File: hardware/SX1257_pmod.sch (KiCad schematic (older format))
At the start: 47 parts, among them J1 Conn_02x06_Odd_Even, J2 SMA_F_RX, J3 SMA_F_TX, U1 SX1257, U2 SC18IS602B, Y1 36MHz 10ppm

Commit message: WIP
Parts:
- added U?: Si514, symbol Si514:Si514
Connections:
- net GND: now also U?.3 (GND)
- net XTB renamed OSC_CLK+
- net OSC_CLK+: now also U?.4 (CLK_+)
- new net +1V8: U?.6 (VDD)
- new net I2C_1V8_SCL: U?.2 (SCL)
- new net I2C_1V8_SDA: U?.1 (SDA)
- no-connect marks 1 -> 2
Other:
- note added: "TODO: 3V3 -> 1V8 LDO"
- note added: "TODO: Level shifting!\nhttps://www.nxp.com/docs/en/application-note/AN10441.pdf"
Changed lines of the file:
@@
 	10850 1000 10850 1100
 NoConn ~ 11550 1900
+$Comp
+L Si514:Si514 U?
+U 1 1 5C7B290D
+P 12400 3950
+F 0 "U?" H 12700 3450 50  0000 C CNN
+F 1 "Si514" H 12650 3550 50  0000 C CNN
+F 2 "" H 11950 4050 50  0001 C CNN
+F 3 "" H 11950 4050 50  0001 C CNN
+	1    12400 3950
+	1    0    0    -1
+$EndComp
+$Comp
+L power:GND #PWR?
+U 1 1 5C7B2B6A
+P 12400 4550
+F 0 "#PWR?" H 12400 4300 50  0001 C CNN
+F 1 "GND" H 12405 4377 50  0000 C CNN
+F 2 "" H 12400 4550 50  0001 C CNN
+F 3 "" H 12400 4550 50  0001 C CNN
+	1    12400 4550
+	1    0    0    -1
+$EndComp
+Wire Wire Line
+	12400 4550 12400 4350
+Wire Wire Line
+	12400 3250 12400 3450
+$Comp
+L power:+1V8 #PWR?
+U 1 1 5C7EB9B9
+P 12400 3250
+F 0 "#PWR?" H 12400 3100 50  0001 C CNN
+F 1 "+1V8" H 12415 3423 50  0000 C CNN
+F 2 "" H 12400 3250 50  0001 C CNN
+F 3 "" H 12400 3250 50  0001 C CNN
+	1    12400 3250
+	1    0    0    -1
+$EndComp
+Text Label 10850 3850 2    50   ~ 0
+I2C_SDA
+Text Label 10850 3950 2    50   ~ 0
+I2C_SCL
+Wire Wire Line
+	11750 3950 11950 3950
+Wire Wire Line
+	11950 3850 11750 3850
+Text Notes 9550 3650 0    50   ~ 0
+TODO: Level shifting!\nhttps://www.nxp.com/docs/en/application-note/AN10441.pdf
+NoConn ~ 12850 3850
+Text Label 13050 3950 0    50   ~ 0
+OSC_CLK+
+Text Label 13700 3950 0    50   ~ 0
+XTB
+Wire Wire Line
+	12850 3950 13700 3950
+Text Label 11750 3850 2    50   ~ 0
+I2C_1V8_SDA
+Text Label 11750 3950 2    50   ~ 0
+I2C_1V8_SCL
+Text Notes 12600 3200 0    50   ~ 0
+TODO: 3V3 -> 1V8 LDO
 $EndSCHEMATC

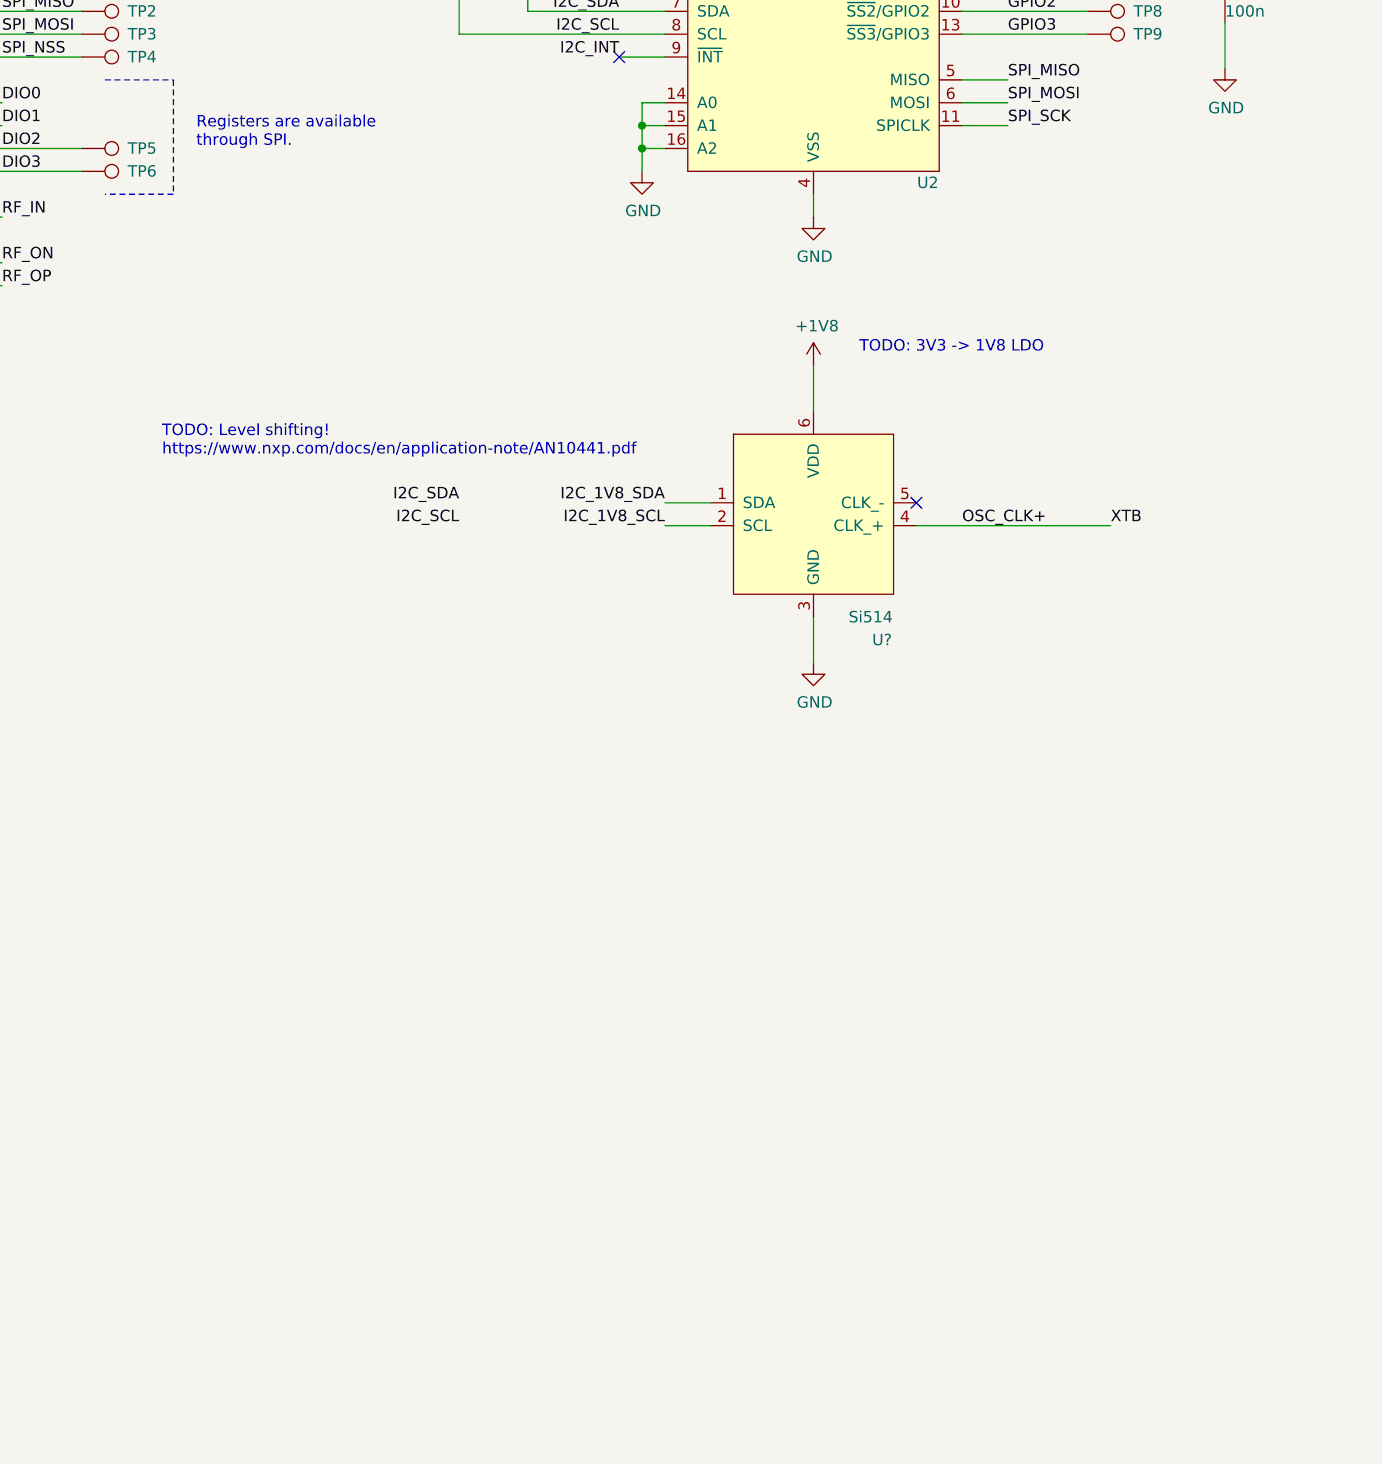
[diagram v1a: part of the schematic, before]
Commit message: Add I2C level shifter
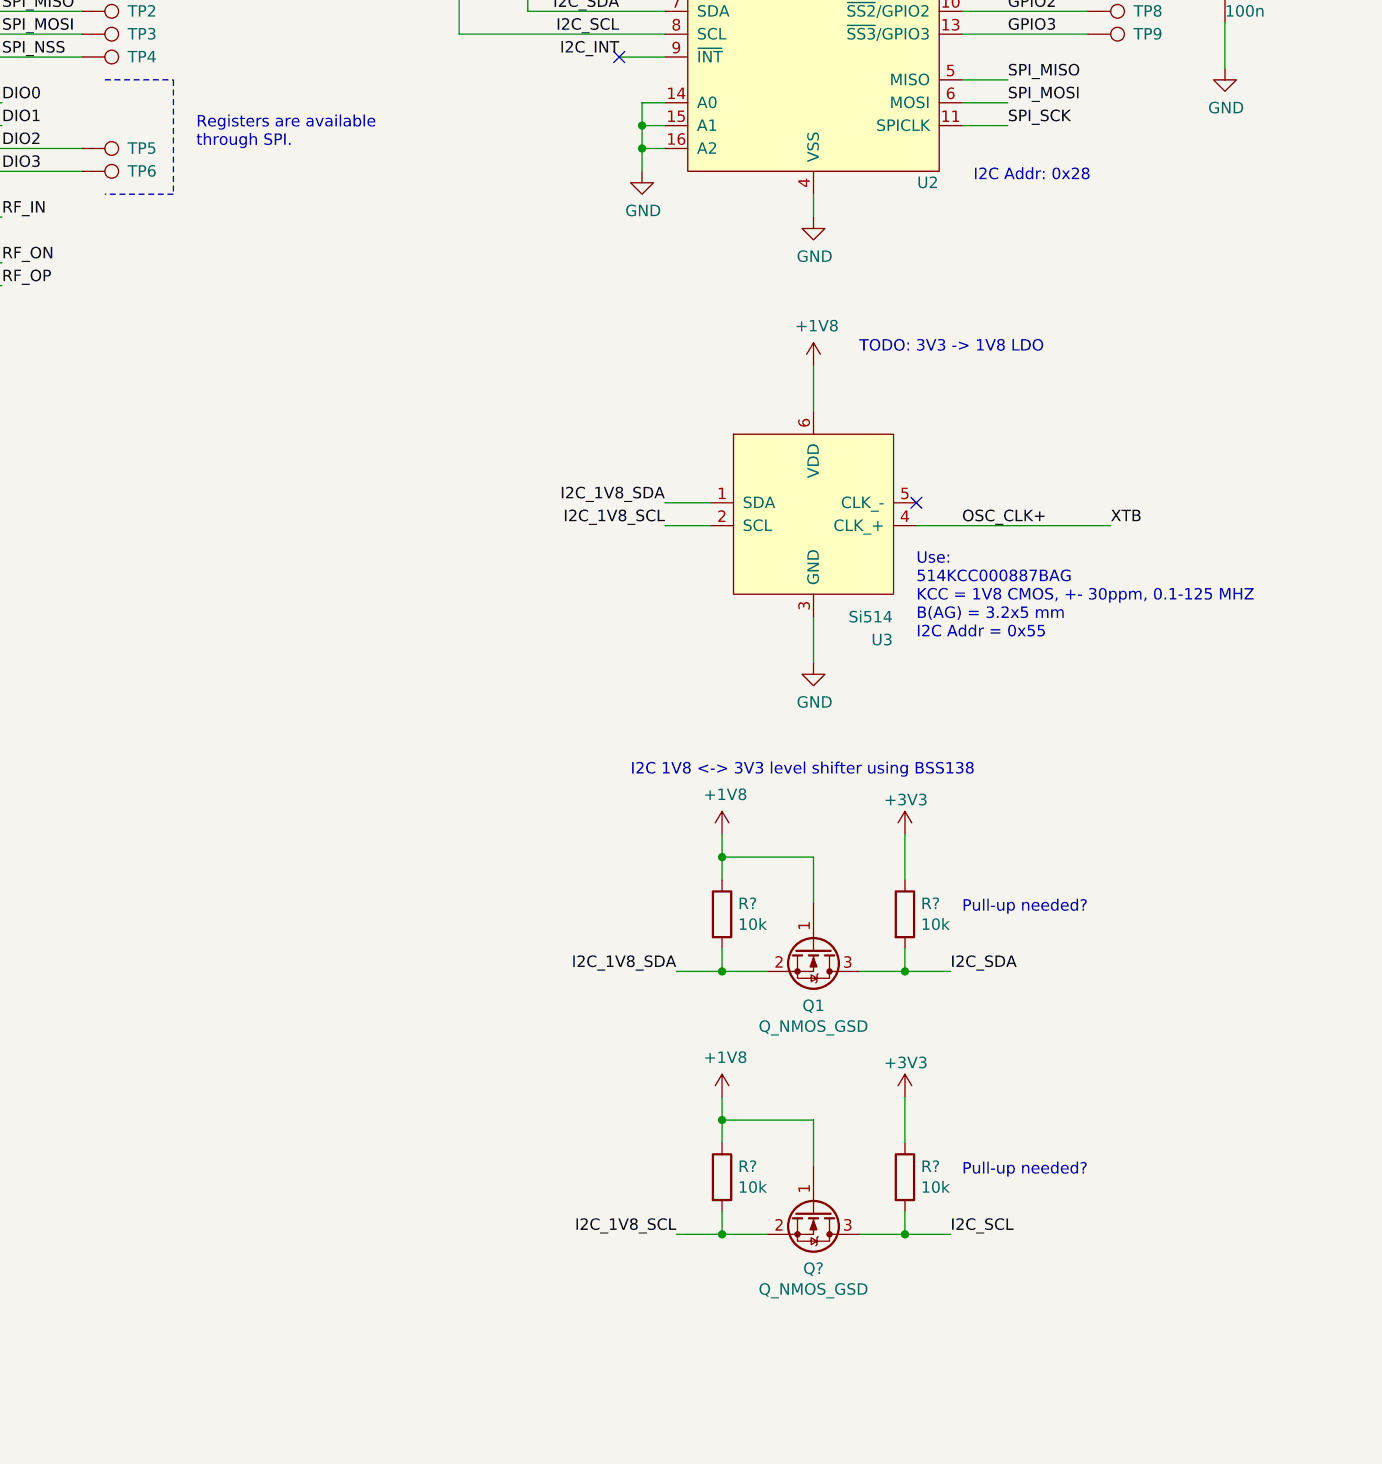
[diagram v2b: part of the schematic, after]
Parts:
- added Q1, Q?: Q_NMOS_GSD, Package_TO_SOT_SMD:SOT-23, symbol Device:Q_NMOS_GSD
- added R? (x4): 10k, Resistor_SMD:R_0603_1608Metric, symbol Device:R
- gave numbers to parts that had none: 1
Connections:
- net +1V8: now also Q1.1 (G), Q?.1 (G), R?.1, R?.1
- net +3V3: now also R?.1, R?.1
- net I2C_1V8_SCL: now also Q?.2 (S), R?.2
- net I2C_1V8_SDA: now also Q1.2 (S), R?.2
- net I2C_SCL: now also Q?.3 (D), R?.2
- net I2C_SDA: now also Q1.3 (D), R?.2
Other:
- note added: "I2C 1V8 <-> 3V3 level shifter using BSS138"
- note added: "I2C Addr: 0x28"
- note added: "Pull-up needed?"
- note added: "Use:\n514KCC000887BAG\nKCC = 1V8 CMOS, +- 30ppm, 0.1-125 MHZ\nB(AG) = 3.2x5 mm\nI2C Addr = 0x55"
- note removed: "TODO: Level shifting!\nhttps://www.nxp.com/docs/en/application-note/AN10441.pdf"
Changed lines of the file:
@@
 NoConn ~ 11550 1900
 $Comp
-L Si514:Si514 U?
+L Si514:Si514 U3
 U 1 1 5C7B290D
 P 12400 3950
-F 0 "U?" H 12700 3450 50  0000 C CNN
+F 0 "U3" H 12700 3450 50  0000 C CNN
 F 1 "Si514" H 12650 3550 50  0000 C CNN
 F 2 "" H 11950 4050 50  0001 C CNN
@@
 $EndComp
 $Comp
-L power:GND #PWR?
+L power:GND #PWR0103
 U 1 1 5C7B2B6A
 P 12400 4550
-F 0 "#PWR?" H 12400 4300 50  0001 C CNN
+F 0 "#PWR0103" H 12400 4300 50  0001 C CNN
 F 1 "GND" H 12405 4377 50  0000 C CNN
 F 2 "" H 12400 4550 50  0001 C CNN
@@
 	12400 3250 12400 3450
 $Comp
-L power:+1V8 #PWR?
+L power:+1V8 #PWR0104
 U 1 1 5C7EB9B9
 P 12400 3250
-F 0 "#PWR?" H 12400 3100 50  0001 C CNN
+F 0 "#PWR0104" H 12400 3100 50  0001 C CNN
 F 1 "+1V8" H 12415 3423 50  0000 C CNN
 F 2 "" H 12400 3250 50  0001 C CNN
@@
 	1    0    0    -1
 $EndComp
-Text Label 10850 3850 2    50   ~ 0
-I2C_SDA
-Text Label 10850 3950 2    50   ~ 0
+Text Label 13000 7050 0    50   ~ 0
 I2C_SCL
 Wire Wire Line
@@
 Wire Wire Line
 	11950 3850 11750 3850
-Text Notes 9550 3650 0    50   ~ 0
-TODO: Level shifting!\nhttps://www.nxp.com/docs/en/application-note/AN10441.pdf
 NoConn ~ 12850 3850
 Text Label 13050 3950 0    50   ~ 0
@@
 Text Notes 12600 3200 0    50   ~ 0
 TODO: 3V3 -> 1V8 LDO
+Text Notes 12850 4450 0    50   ~ 0
+Use:\n514KCC000887BAG\nKCC = 1V8 CMOS, +- 30ppm, 0.1-125 MHZ\nB(AG) = 3.2x5 mm\nI2C Addr = 0x55
+Text Notes 13100 2450 0    50   ~ 0
+I2C Addr: 0x28
+$Comp
+L Device:Q_NMOS_GSD Q1
+U 1 1 5C7BE049
+P 12400 5800
+F 0 "Q1" V 12650 5800 50  0000 C CNN
+F 1 "Q_NMOS_GSD" V 12741 5800 50  0000 C CNN
+F 2 "Package_TO_SOT_SMD:SOT-23" H 12600 5900 50  0001 C CNN
+F 3 "https://www.onsemi.com/pub/Collateral/BSS138-D.PDF" H 12400 5800 50  0001 C CNN
+	1    12400 5800
+	0    1    1    0
+$EndComp
+$Comp
+L Device:R R?
+U 1 1 5C7BEE3D
+P 12000 5650
+F 0 "R?" H 12070 5696 50  0000 L CNN
+F 1 "10k" H 12070 5605 50  0000 L CNN
+F 2 "Resistor_SMD:R_0603_1608Metric" V 11930 5650 50  0001 C CNN
+F 3 "~" H 12000 5650 50  0001 C CNN
+	1    12000 5650
+	1    0    0    -1
+$EndComp
+Wire Wire Line
+	12000 5800 12000 5900
+Wire Wire Line
+	12000 5900 12200 5900
+$Comp
+L Device:R R?
+U 1 1 5C7C922A
+P 12800 5650
+F 0 "R?" H 12870 5696 50  0000 L CNN
+F 1 "10k" H 12870 5605 50  0000 L CNN
+F 2 "Resistor_SMD:R_0603_1608Metric" V 12730 5650 50  0001 C CNN
+F 3 "~" H 12800 5650 50  0001 C CNN
+	1    12800 5650
+	1    0    0    -1
+$EndComp
+Wire Wire Line
+	12800 5800 12800 5900
+Wire Wire Line
+	12800 5900 12600 5900
+Wire Wire Line
+	12400 5600 12400 5400
+Wire Wire Line
+	12400 5400 12000 5400
+Wire Wire Line
+	12000 5400 12000 5500
+$Comp
+L power:+1V8 #PWR?
+U 1 1 5C7DD801
+P 12000 5300
+F 0 "#PWR?" H 12000 5150 50  0001 C CNN
+F 1 "+1V8" H 12015 5473 50  0000 C CNN
+F 2 "" H 12000 5300 50  0001 C CNN
+F 3 "" H 12000 5300 50  0001 C CNN
+	1    12000 5300
+	1    0    0    -1
+$EndComp
+Wire Wire Line
+	12000 5300 12000 5400
+Connection ~ 12000 5400
+$Comp
+L power:+3V3 #PWR?
+U 1 1 5C7E8283
+P 12800 5300
+F 0 "#PWR?" H 12800 5150 50  0001 C CNN
+F 1 "+3V3" H 12700 5450 50  0000 L CNN
+F 2 "" H 12800 5300 50  0001 C CNN
+F 3 "" H 12800 5300 50  0001 C CNN
+	1    12800 5300
+	-1   0    0    -1
+$EndComp
+Wire Wire Line
+	12800 5300 12800 5500
+Text Label 11800 5900 2    50   ~ 0
+I2C_1V8_SDA
+Wire Wire Line
+	11800 5900 12000 5900
+Connection ~ 12000 5900
+Text Label 13000 5900 0    50   ~ 0
+I2C_SDA
+Wire Wire Line
+	13000 5900 12800 5900
+Connection ~ 12800 5900
+$Comp
+L Device:Q_NMOS_GSD Q?
+U 1 1 5C812997
+P 12400 6950
+F 0 "Q?" V 12650 6950 50  0000 C CNN
+F 1 "Q_NMOS_GSD" V 12741 6950 50  0000 C CNN
+F 2 "Package_TO_SOT_SMD:SOT-23" H 12600 7050 50  0001 C CNN
+F 3 "https://www.onsemi.com/pub/Collateral/BSS138-D.PDF" H 12400 6950 50  0001 C CNN
+	1    12400 6950
+	0    1    1    0
+$EndComp
+$Comp
+L Device:R R?
+U 1 1 5C81299E
+P 12000 6800
+F 0 "R?" H 12070 6846 50  0000 L CNN
+F 1 "10k" H 12070 6755 50  0000 L CNN
+F 2 "Resistor_SMD:R_0603_1608Metric" V 11930 6800 50  0001 C CNN
+F 3 "~" H 12000 6800 50  0001 C CNN
+	1    12000 6800
+	1    0    0    -1
+$EndComp
+Wire Wire Line
+	12000 6950 12000 7050
+Wire Wire Line
+	12000 7050 12200 7050
+$Comp
+L Device:R R?
+U 1 1 5C8129A7
+P 12800 6800
+F 0 "R?" H 12870 6846 50  0000 L CNN
+F 1 "10k" H 12870 6755 50  0000 L CNN
+F 2 "Resistor_SMD:R_0603_1608Metric" V 12730 6800 50  0001 C CNN
+F 3 "~" H 12800 6800 50  0001 C CNN
+	1    12800 6800
+	1    0    0    -1
+$EndComp
+Wire Wire Line
+	12800 6950 12800 7050
+Wire Wire Line
+	12800 7050 12600 7050
+Wire Wire Line
+	12400 6750 12400 6550
+Wire Wire Line
+	12400 6550 12000 6550
+Wire Wire Line
+	12000 6550 12000 6650
+$Comp
+L power:+1V8 #PWR?
+U 1 1 5C8129B3
+P 12000 6450
+F 0 "#PWR?" H 12000 6300 50  0001 C CNN
+F 1 "+1V8" H 12015 6623 50  0000 C CNN
+F 2 "" H 12000 6450 50  0001 C CNN
+F 3 "" H 12000 6450 50  0001 C CNN
+	1    12000 6450
+	1    0    0    -1
+$EndComp
+Wire Wire Line
+	12000 6450 12000 6550
+Connection ~ 12000 6550
+$Comp
+L power:+3V3 #PWR?
+U 1 1 5C8129BB
+P 12800 6450
+F 0 "#PWR?" H 12800 6300 50  0001 C CNN
+F 1 "+3V3" H 12700 6600 50  0000 L CNN
+F 2 "" H 12800 6450 50  0001 C CNN
+F 3 "" H 12800 6450 50  0001 C CNN
+	1    12800 6450
+	-1   0    0    -1
+$EndComp
+Wire Wire Line
+	12800 6450 12800 6650
+Wire Wire Line
+	11800 7050 12000 7050
+Connection ~ 12000 7050
+Wire Wire Line
+	13000 7050 12800 7050
+Connection ~ 12800 7050
+Text Label 11800 7050 2    50   ~ 0
+I2C_1V8_SCL
+Text Notes 13050 5650 0    50   ~ 0
+Pull-up needed?
+Text Notes 11600 5050 0    50   ~ 0
+I2C 1V8 <-> 3V3 level shifter using BSS138
+Text Notes 13050 6800 0    50   ~ 0
+Pull-up needed?
 $EndSCHEMATC
